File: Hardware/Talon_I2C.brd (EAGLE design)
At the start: 140 x 19 mm, 93 parts, among them J1 CONN_TALON_REMOTE, J2 CONN_I2C_LOGGER, J3 CONN_I2C_LOGGER, J4 CONN_I2C_LOGGER, J5 CONN_I2C_LOGGER, Q1 2N7002, Q2 2N7002, Q3 2N7002, Q4 2N7002, Q5 AO3419, Q6 AO3419, Q7 AO3419, Q8 AO3419, U1 SN74HC04, U10 74HC4852, U11 SN74LVC1G3157SC70, U12 MCP3421A3, U13 FXMAR2102UMLP, U14 PCA9617WSON, U15 PCA9617WSON, U16 PCA9617WSON, U17 PCA9617WSON, U18 SN74AUP1G08DCK, U19 SN74AUP1G08DCK, U2 CD4044, U20 SN74AUP1G08DCK, U21 SN74AUP1G08DCK, U3 SIP32431TDFN, U4 INA4180A2, U5 MAX9034TSSOP, U6 SN74AC08, U7 24AA02SOT23, U8 MCP23018QFN, U9 PCA9536DFN

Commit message: v2.0 update
Fixed physical overlap in current limit circuit, fixed connector pinout
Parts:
- moved C15 0.51 mm to (-46.7, 11.3)
- moved R32 0.51 mm to (-43.7, 11.3)
- moved R28 0.38 mm to (-31.5, 9.40)
- moved R29 0.38 mm to (-30.4, 9.40)
- moved R30 0.38 mm to (-32.6, 9.40)
- moved U1 0.38 mm to (-36.7, 9.14)
- moved U2 0.38 mm to (-44.5, 8.13)
- moved U6 0.38 mm to (-36.7, 4.19)
- moved R33 0.25 mm to (-40.5, 13.1)
- moved C16 0.25 mm to (-40.5, 14.2)
- moved U5 0.25 mm to (-45.6, 14.4)
- moved U19 0.25 mm to (-25.8, 8.89)
- moved R27 0.13 mm to (-34.5, 12.2)
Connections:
- net GND: now also J2.4, J3.4, J4.4, J5.4; no longer J2.3, J3.3, J4.3, J5.3
- net PORT1_SCL: now also J2.3; no longer J2.4
- net PORT1_SDA: now also J2.1; no longer J2.2
- net PORT2_SCL: now also J3.3; no longer J3.4
- net PORT2_SDA: now also J3.1; no longer J3.2
- net PORT3_SCL: now also J4.3; no longer J4.4
- net PORT3_SDA: now also J4.1; no longer J4.2
- net PORT4_SCL: now also J5.3; no longer J5.4
- net PORT4_SDA: now also J5.1; no longer J5.2
- net VPORT1_OUT: now also J2.2; no longer J2.1
- net VPORT2_OUT: now also J3.2; no longer J3.1
- net VPORT3_OUT: now also J4.2; no longer J4.1
- net VPORT4_OUT: now also J5.2; no longer J5.1
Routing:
- net VPORT2_OUT: track 56.6 -> 62.7 mm
- net MOS_CTRL3: track 82.2 -> 77.0 mm
- net GND: track 386.7 -> 391.3 mm
- net PORT1_SCL: track 6.90 -> 9.86 mm
- net PORT4_SCL: track 15.1 -> 17.8 mm
- net VPORT4_OUT: track 189.2 -> 191.6 mm
- net VPORT3_OUT: track 109.2 -> 111.3 mm
- net PORT1_SDA: track 4.21 -> 6.14 mm
- net PORT2_SCL: track 9.30 -> 7.38 mm
- net PORT4_SDA: track 10.9 -> 12.6 mm
- net !I2C_OB_EN: track 127.9 -> 129.5 mm
- net PORT2_SDA: track 7.10 -> 5.63 mm
- net VPORT1_OUT: track 128.3 -> 126.8 mm
- net PORT3_SCL: track 10.5 -> 9.04 mm
- net DATA4_EN: track 88.1 -> 89.3 mm
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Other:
- board text added: "Talon - I2C v2.0 Bobby Schulz"
- board text removed: "Talon - I2C v1.1 Bobby Schulz"

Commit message: Part number updates
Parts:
- C14, C15, C16, C17: value 0.1uF -> DNP
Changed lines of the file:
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@@
 <attribute name="VALUE_PART" value="1k" x="-43.688" y="17.399" size="1.778" layer="27" rot="R180" display="off"/>
 </element>
-<element name="C14" library="bschulz_passives" package="C0402" value="0.1uF" x="-46.736" y="17.399" smashed="yes" rot="R180">
-<attribute name="DIGIKEY" value="490-4759-1-ND" x="-46.736" y="17.399" size="1.778" layer="27" rot="R180" display="off"/>
-<attribute name="MF" value="Murata" x="-46.736" y="17.399" size="1.778" layer="27" rot="R180" display="off"/>
-<attribute name="MPN" value="GCM155R71C104KA55D" x="-46.736" y="17.399" size="1.778" layer="27" rot="R180" display="off"/>
+<element name="C14" library="bschulz_passives" package="C0402" value="DNP" x="-46.736" y="17.399" smashed="yes" rot="R180">
+<attribute name="DIGIKEY" value="DNP" x="-46.736" y="17.399" size="1.778" layer="27" rot="R180" display="off"/>
+<attribute name="MF" value="N/A" x="-46.736" y="17.399" size="1.778" layer="27" rot="R180" display="off"/>
+<attribute name="MPN" value="DNP" x="-46.736" y="17.399" size="1.778" layer="27" rot="R180" display="off"/>
 <attribute name="NAME" x="-46.736" y="18.288" size="0.6096" layer="25" font="vector" ratio="15" rot="R180" align="center"/>
 <attribute name="VALUE" x="-46.736" y="18.415" size="0.6096" layer="27" font="vector" ratio="15" rot="R180" align="center"/>
@@
 <attribute name="VALUE_PART" value="1k" x="-43.688" y="7.493" size="1.778" layer="27" rot="R180" display="off"/>
 </element>
-<element name="C15" library="bschulz_passives" package="C0402" value="0.1uF" x="-46.736" y="11.303" smashed="yes" rot="R180">
-<attribute name="DIGIKEY" value="490-4759-1-ND" x="-46.736" y="15.113" size="1.778" layer="27" rot="R180" display="off"/>
-<attribute name="MF" value="Murata" x="-46.736" y="15.113" size="1.778" layer="27" rot="R180" display="off"/>
-<attribute name="MPN" value="GCM155R71C104KA55D" x="-46.736" y="15.113" size="1.778" layer="27" rot="R180" display="off"/>
+<element name="C15" library="bschulz_passives" package="C0402" value="DNP" x="-46.736" y="11.303" smashed="yes" rot="R180">
+<attribute name="DIGIKEY" value="DNP" x="-46.736" y="15.113" size="1.778" layer="27" rot="R180" display="off"/>
+<attribute name="MF" value="N/A" x="-46.736" y="15.113" size="1.778" layer="27" rot="R180" display="off"/>
+<attribute name="MPN" value="DNP" x="-46.736" y="15.113" size="1.778" layer="27" rot="R180" display="off"/>
 <attribute name="NAME" x="-48.387" y="11.049" size="0.6096" layer="25" font="vector" ratio="15" rot="R270" align="center"/>
 <attribute name="VALUE" x="-46.736" y="12.319" size="0.6096" layer="27" font="vector" ratio="15" rot="R180" align="center"/>
@@
 <attribute name="VALUE_PART" value="1k" x="-40.513" y="9.271" size="1.778" layer="27" rot="R180" display="off"/>
 </element>
-<element name="C16" library="bschulz_passives" package="C0402" value="0.1uF" x="-40.513" y="14.224" smashed="yes">
-<attribute name="DIGIKEY" value="490-4759-1-ND" x="-40.513" y="10.414" size="1.778" layer="27" display="off"/>
-<attribute name="MF" value="Murata" x="-40.513" y="10.414" size="1.778" layer="27" display="off"/>
-<attribute name="MPN" value="GCM155R71C104KA55D" x="-40.513" y="10.414" size="1.778" layer="27" display="off"/>
+<element name="C16" library="bschulz_passives" package="C0402" value="DNP" x="-40.513" y="14.224" smashed="yes">
+<attribute name="DIGIKEY" value="DNP" x="-40.513" y="10.414" size="1.778" layer="27" display="off"/>
+<attribute name="MF" value="N/A" x="-40.513" y="10.414" size="1.778" layer="27" display="off"/>
+<attribute name="MPN" value="DNP" x="-40.513" y="10.414" size="1.778" layer="27" display="off"/>
 <attribute name="NAME" x="-39.116" y="14.224" size="0.6096" layer="25" font="vector" ratio="15" rot="R90" align="center"/>
 <attribute name="VALUE" x="-40.513" y="13.208" size="0.6096" layer="27" font="vector" ratio="15" align="center"/>
@@
 <attribute name="VALUE_PART" value="1k" x="-40.513" y="13.335" size="1.778" layer="27" rot="R180" display="off"/>
 </element>
-<element name="C17" library="bschulz_passives" package="C0402" value="0.1uF" x="-40.513" y="16.002" smashed="yes">
-<attribute name="DIGIKEY" value="490-4759-1-ND" x="-40.513" y="12.192" size="1.778" layer="27" display="off"/>
-<attribute name="MF" value="Murata" x="-40.513" y="12.192" size="1.778" layer="27" display="off"/>
-<attribute name="MPN" value="GCM155R71C104KA55D" x="-40.513" y="12.192" size="1.778" layer="27" display="off"/>
+<element name="C17" library="bschulz_passives" package="C0402" value="DNP" x="-40.513" y="16.002" smashed="yes">
+<attribute name="DIGIKEY" value="DNP" x="-40.513" y="12.192" size="1.778" layer="27" display="off"/>
+<attribute name="MF" value="N/A" x="-40.513" y="12.192" size="1.778" layer="27" display="off"/>
+<attribute name="MPN" value="DNP" x="-40.513" y="12.192" size="1.778" layer="27" display="off"/>
 <attribute name="NAME" x="-39.116" y="16.002" size="0.6096" layer="25" font="vector" ratio="15" rot="R90" align="center"/>
 <attribute name="VALUE" x="-40.513" y="14.986" size="0.6096" layer="27" font="vector" ratio="15" align="center"/>

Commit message: Updated EEPROM part
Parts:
- U7: value 24AA02SOT23 -> AT24MAC602SOT23
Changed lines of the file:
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@@
 <attribute name="VALUE" x="57.45" y="1.227" size="1.27" layer="28" font="vector" ratio="15" rot="MR0" align="center"/>
 </element>
-<element name="U7" library="bschulz" package="SOT23-5" value="24AA02SOT23" x="-18.796" y="17.018" smashed="yes" rot="R90">
-<attribute name="DIGIKEY" value="24AA025E64T-I/OTCT-ND" x="-18.796" y="17.018" size="1.778" layer="27" rot="R90" display="off"/>
-<attribute name="DISP" value="24AA025E64" x="-18.796" y="17.018" size="1.778" layer="27" rot="R90" display="off"/>
+<element name="U7" library="bschulz" package="SOT23-5" value="AT24MAC602SOT23" x="-18.796" y="17.018" smashed="yes" rot="R90">
+<attribute name="DIGIKEY" value="AT24MAC602-STUM-TCT-ND" x="-18.796" y="17.018" size="1.778" layer="27" rot="R90" display="off"/>
+<attribute name="DISP" value="AT24MAC602" x="-18.796" y="17.018" size="1.778" layer="27" rot="R90" display="off"/>
 <attribute name="MF" value="Microchip" x="-18.796" y="17.018" size="1.778" layer="27" rot="R90" display="off"/>
-<attribute name="MOUSER" value="24AA025E64T-I/OTCT-ND" x="-18.796" y="17.018" size="1.778" layer="27" rot="R90" display="off"/>
-<attribute name="MPN" value="24AA025E64T-I/OT" x="-18.796" y="17.018" size="1.778" layer="27" rot="R90" display="off"/>
+<attribute name="MPN" value="AT24MAC602-STUM-T" x="-18.796" y="17.018" size="1.778" layer="27" rot="R90" display="off"/>
 <attribute name="NAME" x="-20.066" y="17.018" size="0.6096" layer="25" font="vector" ratio="15" rot="R270" align="center"/>
 <attribute name="VALUE" x="-18.923" y="19.304" size="0.6096" layer="27" font="vector" ratio="15" rot="R180" align="center"/>

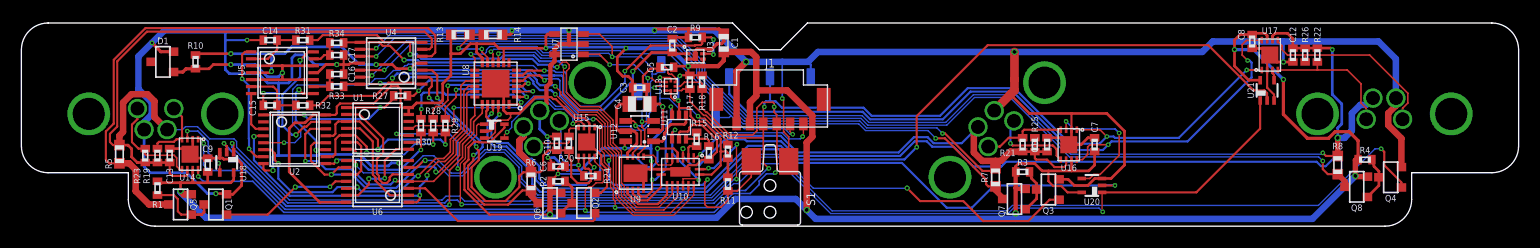
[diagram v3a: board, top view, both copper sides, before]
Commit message: v2.1 updates
Updates made to schematic and layout, boards sent to fab
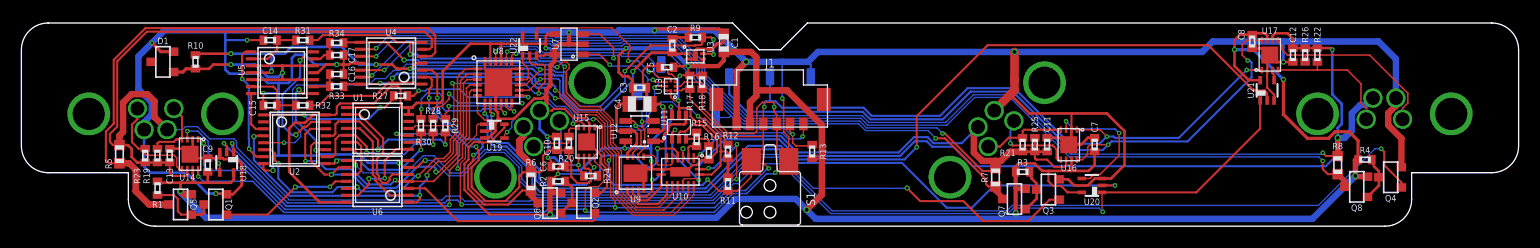
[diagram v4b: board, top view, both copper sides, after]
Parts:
- removed R14: 49.9k, bschulz_passives:R0603
- added U22: SN74AUP1G32DCK, bschulz:DCK_R-PDSO-G5
- R13: value 110k -> 100k; device bschulz_passives:R0603 -> bschulz_passives:R0402
- U8: value MCP23018QFN -> PCAL9535AQFN
- moved R13 34.7 mm to (3.94, 6.99), turned to 270 degrees
- moved U8 0.28 mm to (-25.4, 13.5), turned to 0 degrees
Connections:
- removed net N$14: R13.1, R14.2, U8.11
- new net LOOPBACK_EN: U22.1, U8.16
- new net N$7: U13.5, U22.4
- net 3V3: now also U22.5, U8.21, U8.23; no longer U8.12, U8.8
- net DATA1_EN: now also U8.5; no longer U8.19
- net DATA2_EN: now also U8.6; no longer U8.20
- net DATA3_EN: now also U8.7; no longer U8.21
- net DATA4_EN: now also U8.8; no longer U8.22
- net EN1: now also U8.1; no longer U8.15
- net EN2: now also U8.2; no longer U8.16
- net EN3: now also U8.3; no longer U8.17
- net EN4: now also U8.4; no longer U8.18
- net FAULT1_SENSE: now also U8.10; no longer U8.24
- net FAULT2_SENSE: now also U8.11; no longer U8.1
- net FAULT3_SENSE: now also U8.12; no longer U8.2
- net FAULT4_SENSE: now also U8.13; no longer U8.3
- net GND: now also U22.3, U8.18, U8.24, U8.9; no longer R14.1, U8.23
- net I2C_OB_EN: now also U22.2; no longer U13.5
- net INTB: now also R13.1, U8.22; no longer U8.13
- net POS_DETECT: now also U8.14; no longer U8.4
- net SCL_OB: now also U8.19; no longer U8.9
- net SDA_OB: now also U8.20; no longer U8.10
- net SENSE_EN: now also U8.15; no longer U8.5
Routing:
- net N$7: track 0.00 -> 16.4 mm, vias 0 -> 2
- net N$14: track 6.75 -> 0.00 mm, vias 2 -> 0
- net GND: track 391.3 -> 397.0 mm, vias 20 -> 19
- net POS_DETECT: track 36.5 -> 32.6 mm
- net I2C_OB_EN: track 52.4 -> 56.3 mm
- net LOOPBACK_EN: track 0.00 -> 3.20 mm
- net FAULT3_SENSE: track 13.7 -> 11.4 mm
- net FAULT2_SENSE: track 11.0 -> 8.89 mm
- net SCL_OB: track 30.6 -> 28.8 mm
- net EN4: track 27.3 -> 28.9 mm
- net DATA1_EN: track 35.2 -> 36.7 mm
- net EN3: track 28.0 -> 29.5 mm
- net EN2: track 34.6 -> 36.1 mm
- net SDA_OB: track 35.6 -> 34.2 mm
- net EN1: track 31.4 -> 32.7 mm
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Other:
- board text added: "Talon - I2C v2.1 Bobby Schulz"
- board text removed: "Talon - I2C v2.0 Bobby Schulz"
